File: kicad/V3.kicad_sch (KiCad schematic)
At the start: 2 parts, among them U1 SuperMini nRF52840

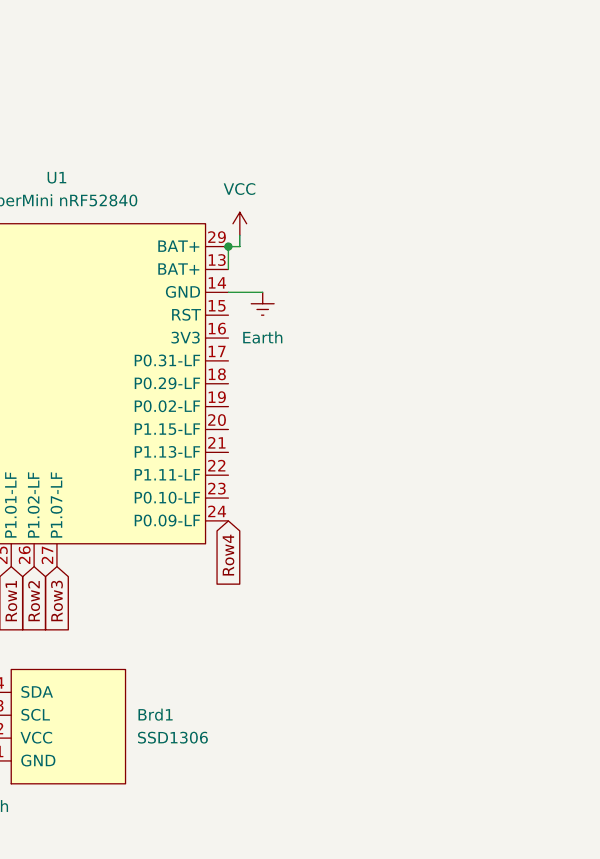
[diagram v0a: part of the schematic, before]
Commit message: change to esp32
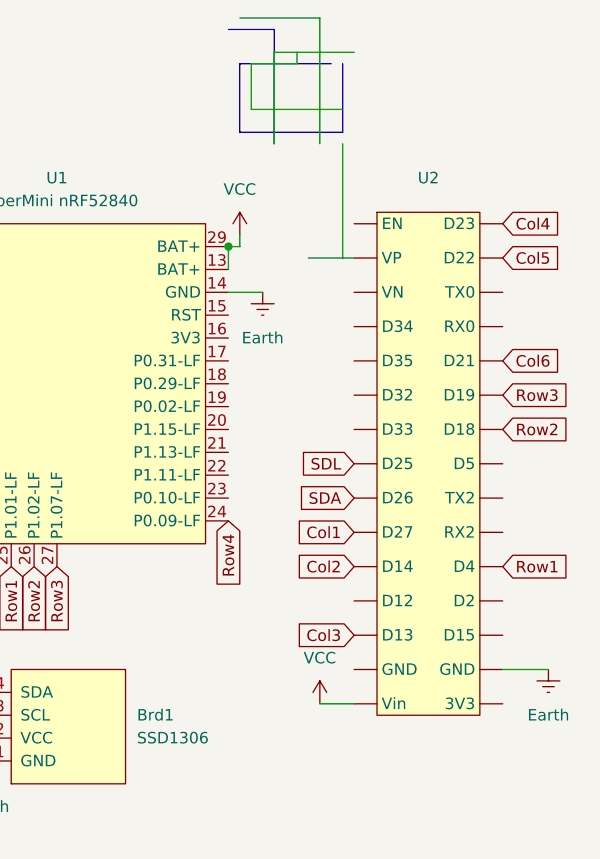
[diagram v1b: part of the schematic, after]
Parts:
- added U2: ~, symbol Library:Esp32_Dev_Module
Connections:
- net Col1: now also U2. (3V3)
- net Col2: now also U2. (3V3)
- net Col3: now also U2. (3V3)
- net Col4: now also U2. (3V3)
- net Col5: now also U2. (3V3)
- net Col6: now also U2. (3V3)
- net Earth: now also U2. (3V3)
- net Row1: now also U2. (3V3)
- net Row2: now also U2. (3V3)
- net Row3: now also U2. (3V3)
- net SDA: now also U2. (3V3)
- net SDL: now also U2. (3V3)
- net VCC: now also U2. (3V3)
